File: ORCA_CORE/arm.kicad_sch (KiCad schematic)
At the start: 0 parts

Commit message: add power registers to power_board gate driver
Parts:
- added C10: 22u25V, Capacitor_SMD:C_0805_2012Metric_Pad1.18x1.45mm_HandSolder, symbol Device:C
- added C9: 10u/50V, Capacitor_SMD:C_1206_3216Metric_Pad1.33x1.80mm_HandSolder, symbol Device:C
- added D4: enable_arm, LED_SMD:LED_0603_1608Metric_Pad1.05x0.95mm_HandSolder, symbol Device:LED_Filled
- added D5: power_input_arm, LED_SMD:LED_0603_1608Metric_Pad1.05x0.95mm_HandSolder, symbol Device:LED_Filled
- added D6: CUHS20560, Diode:Diode_US2H, symbol Device:D_Schottky
- added J26: Vin_motor, Connector_JST:JST_XH_S2B-XH-A_1x02_P2.50mm_Horizontal, symbol Connector_Generic:Conn_01x02
- added J27: servo_0, symbol Connector:Conn_01x03_Pin
- added J28: servo_1, symbol Connector:Conn_01x03_Pin
- added J29: servo_2, symbol Connector:Conn_01x03_Pin
- added J30: servo_3, symbol Connector:Conn_01x03_Pin
- added Q3: TJ60S04M3L, toshiba:2-7M1A, symbol Simulation_SPICE:PMOS
- added R26: 10k, Resistor_SMD:R_0603_1608Metric_Pad0.98x0.95mm_HandSolder, symbol Device:R
- added R27, R28: 1k, Resistor_SMD:R_0603_1608Metric_Pad0.98x0.95mm_HandSolder, symbol Device:R
- added R29, R32, R39, R42, R45: 100, symbol Device:R
- added R30, R33, R36, R40, R41, R43, R44, R46, R50: 2.2k, symbol Device:R
- added R31: 47, symbol Device:R
- added U11, U12, U13, U15, U16: TLP293, Package_SO:SOIC-4_4.55x2.6mm_P1.27mm, symbol Isolator:TLP293
- added U17: AZ1117-3.3, Package_TO_SOT_SMD:SOT-223-3_TabPin2, symbol mylib:AZ1117-3.3V
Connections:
- new net: R29.2, R30.1, U11.1
- new net: J28.3 (Pin_3), U13.3
- new net: D5.2 (A), R28.1
- new net: R32.2, R33.1, U12.1
- new net: J27.3 (Pin_3), U12.3
- new net: R36.1, U12.4
- new net: R44.1, U15.4
- new net: D4.2 (A), R27.2
- new net: Q3.2 (G), R26.1, U11.3
- new net: R31.1, U11.4
- new net: R39.2, R40.1, U13.1
- new net: R41.1, U13.4
- new net: J30.3 (Pin_3), U16.3
- new net: R42.2, R43.1, U15.1
- new net: J29.3 (Pin_3), U15.3
- new net: R50.1, U16.4
- new net: R45.2, R46.1, U16.1
- new net +3V3: C10.1, D6.2 (A), R36.2, R41.2, R44.2, R50.2, U17.2 (Vout)
- new net +6V: J26.2 (Pin_2)
- new net +6V_in: C9.1, D6.1 (K), Q3.3 (S), R28.2, R31.2, U17.3 (Vin)
- new net +6V_out: J27.2 (Pin_2), J28.2 (Pin_2), J29.2 (Pin_2), J30.2 (Pin_2), Q3.1 (D), R27.1
- new net GND: C10.2, C9.2, D4.1 (K), D5.1 (K), J26.1 (Pin_1), J27.1 (Pin_1), J28.1 (Pin_1), J29.1 (Pin_1), J30.1 (Pin_1), R26.2, U17.1 (GND)
- new net GND1: U11.2, U12.2, U13.2, U15.2, U16.2
- new net Vin_cpu: R30.2, R33.2, R40.2, R43.2, R46.2
- new net enable_arm: R29.1
- new net servo_0: R32.1
- new net servo_1: R39.1
- new net servo_2: R42.1
- new net servo_3: R45.1
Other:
- note added: "4 motor inputs"
- note added: "enabler"
- note added: "power"
- note added: "regulator"

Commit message: almost completed CORE
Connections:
- net +6V is gone; now on net +6V_in: J26.2 (Pin_2)
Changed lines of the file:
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@@
 	)
 	(global_label "+6V_out"
-		(shape input)
+		(shape output)
 		(at 170.18 64.77 0)
 		(fields_autoplaced yes)
@@
 	)
 	(global_label "+3V3"
-		(shape input)
+		(shape output)
 		(at 259.08 41.91 0)
 		(fields_autoplaced yes)
@@
 		)
 	)
-	(global_label "+6V"
+	(global_label "+6V_in"
 		(shape input)
 		(at 53.34 71.12 0)
@@
 		)
 		(property "Intersheetrefs" "${INTERSHEET_REFS}"
-			(at 60.1957 71.12 0)
+			(at 62.9171 71.12 0)
 			(effects
 				(font

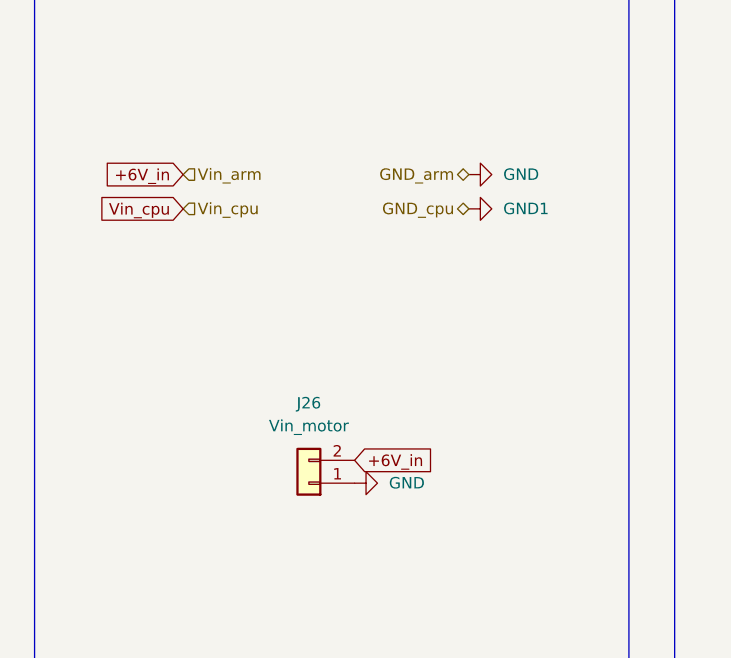
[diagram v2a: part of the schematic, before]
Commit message: complete attaching footprint of CORE
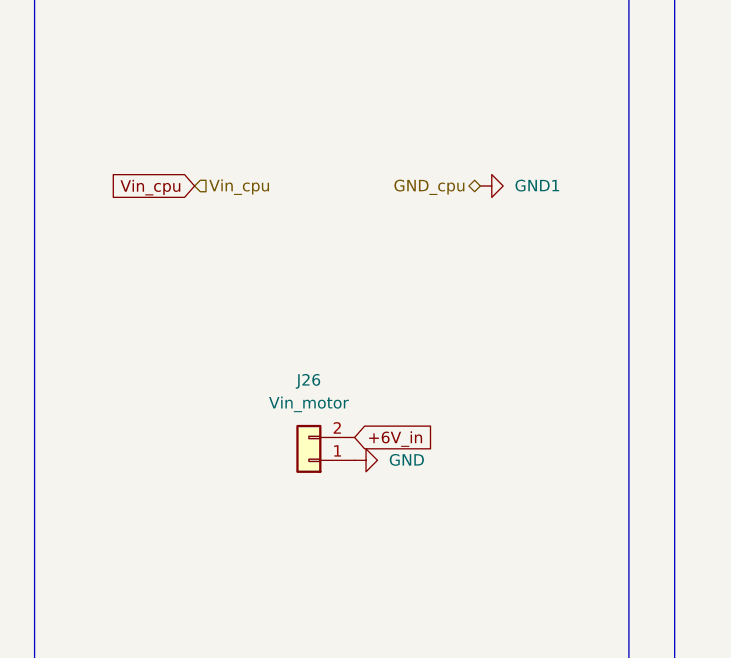
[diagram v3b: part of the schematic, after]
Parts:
- J27, J28, J29, J30: footprint (none) -> Connector_PinHeader_2.54mm:PinHeader_1x03_P2.54mm_Horizontal
- R29, R30, R31, R32, R33, R36, R39, R40, R41, R42, R43, R44, R45, R46, R50: footprint (none) -> Resistor_SMD:R_0603_1608Metric_Pad0.98x0.95mm_HandSolder
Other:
- moved on the sheet: J26
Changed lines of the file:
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@@
 	(global_label "Vin_cpu"
 		(shape input)
-		(at 34.29 43.18 180)
+		(at 35.56 40.64 180)
 		(fields_autoplaced yes)
 		(effects
@@
 		)
 		(property "Intersheetrefs" "${INTERSHEET_REFS}"
-			(at 24.1082 43.18 0)
+			(at 25.3782 40.64 0)
 			(effects
 				(font
@@
 		)
 	)
-	(global_label "+6V_in"
-		(shape input)
-		(at 34.29 39.37 180)
-		(fields_autoplaced yes)
-		(effects
-			(font
-				(size 1.27 1.27)
-			)
-			(justify right)
-		)
-		(property "Intersheetrefs" "${INTERSHEET_REFS}"
-			(at 24.7129 39.37 0)
-			(effects
-				(font
-					(size 1.27 1.27)
-				)
-				(justify right)
-				(hide yes)
-			)
-		)
-	)
 	(global_label "Vin_cpu"
 		(shape input)
@@
 	(global_label "+6V_in"
 		(shape input)
-		(at 53.34 71.12 0)
+		(at 53.34 68.58 0)
 		(fields_autoplaced yes)
 		(effects
@@
 		)
 		(property "Intersheetrefs" "${INTERSHEET_REFS}"
-			(at 62.9171 71.12 0)
+			(at 62.9171 68.58 0)
 			(effects
 				(font
@@
 		)
 	)
-	(hierarchical_label "GND_arm"
-		(shape bidirectional)
-		(at 66.04 39.37 180)
-		(fields_autoplaced yes)
-		(effects
-			(font
-				(size 1.27 1.27)
-			)
-			(justify right)
-		)
-	)
 	(hierarchical_label "GND_cpu"
 		(shape bidirectional)
-		(at 66.04 43.18 180)
+		(at 67.31 40.64 180)
 		(fields_autoplaced yes)
 		(effects
@@
 		)
 	)
-	(hierarchical_label "Vin_arm"
-		(shape input)
-		(at 34.29 39.37 0)
-		(fields_autoplaced yes)
-		(effects
-			(font
-				(size 1.27 1.27)
-			)
-			(justify left)
-		)
-	)
 	(hierarchical_label "Vin_cpu"
 		(shape input)
-		(at 34.29 43.18 0)
+		(at 35.56 40.64 0)
 		(fields_autoplaced yes)
 		(effects
@@
 			)
 		)
-		(property "Footprint" ""
+		(property "Footprint" "Resistor_SMD:R_0603_1608Metric_Pad0.98x0.95mm_HandSolder"
 			(at 131.318 35.56 90)
 			(effects
@@
 	(symbol
 		(lib_id "power:GND")
-		(at 66.04 39.37 90)
-		(unit 1)
-		(exclude_from_sim no)
-		(in_bom yes)
-		(on_board yes)
-		(dnp no)
-		(fields_autoplaced yes)
-		(property "Reference" "#PWR061"
-			(at 72.39 39.37 0)
-			(effects
-				(font
-					(size 1.27 1.27)
-				)
-				(hide yes)
-			)
-		)
-		(property "Value" "GND"
-			(at 69.85 39.3699 90)
-			(effects
-				(font
-					(size 1.27 1.27)
-				)
-				(justify right)
-			)
-		)
-		(property "Footprint" ""
-			(at 66.04 39.37 0)
-			(effects
-				(font
-					(size 1.27 1.27)
-				)
-				(hide yes)
-			)
-		)
-		(property "Datasheet" ""
-			(at 66.04 39.37 0)
-			(effects
-				(font
-					(size 1.27 1.27)
-				)
-				(hide yes)
-			)
-		)
-		(property "Description" "Power symbol creates a global label with name \"GND\" , ground"
-			(at 66.04 39.37 0)
-			(effects
-				(font
-					(size 1.27 1.27)
-				)
-				(hide yes)
-			)
-		)
-		(pin "1"
-		)
-		(instances
-			(project "ORCA_CORE"
-				(path "/895d6bb7-4008-488b-a34b-0077e9f7e4a1/f4046d1b-97e2-423b-a39b-40122b0e9f7a"
-					(reference "#PWR061")
-					(unit 1)
-				)
-			)
-		)
-	)
-	(symbol
-		(lib_id "power:GND")
 		(at 215.9 154.94 270)
 		(unit 1)
@@
 			)
 		)
-		(property "Footprint" ""
+		(property "Footprint" "Connector_PinHeader_2.54mm:PinHeader_1x03_P2.54mm_Horizontal"
 			(at 116.84 152.4 0)
 			(effects
@@
 			)
 		)
-		(property "Footprint" ""
+		(property "Footprint" "Resistor_SMD:R_0603_1608Metric_Pad0.98x0.95mm_HandSolder"
 			(at 208.28 118.618 90)
 			(effects
@@
 			)
 		)
-		(property "Footprint" ""
+		(property "Footprint" "Resistor_SMD:R_0603_1608Metric_Pad0.98x0.95mm_HandSolder"
 			(at 123.19 43.688 90)
 			(effects
@@
 			)
 		)
-		(property "Footprint" ""
+		(property "Footprint" "Resistor_SMD:R_0603_1608Metric_Pad0.98x0.95mm_HandSolder"
 			(at 83.058 110.49 90)
 			(effects
@@
 			)
 		)
-		(property "Footprint" ""
+		(property "Footprint" "Resistor_SMD:R_0603_1608Metric_Pad0.98x0.95mm_HandSolder"
 			(at 152.4 43.688 90)
 			(effects
@@
 			)
 		)
-		(property "Footprint" ""
+		(property "Footprint" "Resistor_SMD:R_0603_1608Metric_Pad0.98x0.95mm_HandSolder"
 			(at 74.93 118.618 90)
 			(effects
@@
 			)
 		)
-		(property "Footprint" ""
+		(property "Footprint" "Connector_PinHeader_2.54mm:PinHeader_1x03_P2.54mm_Horizontal"
 			(at 220.98 152.4 0)
 			(effects
@@
 	(symbol
 		(lib_id "power:GND1")
-		(at 66.04 43.18 90)
+		(at 67.31 40.64 90)
 		(unit 1)
 		(exclude_from_sim no)
@@
 		(fields_autoplaced yes)
 		(property "Reference" "#PWR062"
-			(at 72.39 43.18 0)
+			(at 73.66 40.64 0)
 			(effects
 				(font
@@
 		)
 		(property "Value" "GND1"
-			(at 69.85 43.1799 90)
+			(at 71.12 40.6399 90)
 			(effects
 				(font
@@
 		)
 		(property "Footprint" ""
-			(at 66.04 43.18 0)
+			(at 67.31 40.64 0)
 			(effects
 				(font
@@
 		)
 		(property "Datasheet" ""
-			(at 66.04 43.18 0)
+			(at 67.31 40.64 0)
 			(effects
 				(font
@@
 		)
 		(property "Description" "Power symbol creates a global label with name \"GND1\" , ground"
-			(at 66.04 43.18 0)
+			(at 67.31 40.64 0)
 			(effects
 				(font
@@
 			)
 		)
-		(property "Footprint" ""
+		(property "Footprint" "Resistor_SMD:R_0603_1608Metric_Pad0.98x0.95mm_HandSolder"
 			(at 74.93 146.558 90)
 			(effects
@@
 			)
 		)
-		(property "Footprint" ""
+		(property "Footprint" "Connector_PinHeader_2.54mm:PinHeader_1x03_P2.54mm_Horizontal"
 			(at 220.98 124.46 0)
 			(effects
@@
 			)
 		)
-		(property "Footprint" ""
+		(property "Footprint" "Resistor_SMD:R_0603_1608Metric_Pad0.98x0.95mm_HandSolder"
 			(at 208.28 146.558 90)
 			(effects
@@
 	(symbol
 		(lib_id "power:GND")
-		(at 53.34 73.66 90)
+		(at 53.34 71.12 90)
 		(unit 1)
 		(exclude_from_sim no)
@@
 		(fields_autoplaced yes)
 		(property "Reference" "#PWR060"
-			(at 59.69 73.66 0)
+			(at 59.69 71.12 0)
 			(effects
 				(font
@@
 		)
 		(property "Value" "GND"
-			(at 57.15 73.6599 90)
+			(at 57.15 71.1199 90)
 			(effects
 				(font
@@
 		)
 		(property "Footprint" ""
-			(at 53.34 73.66 0)
+			(at 53.34 71.12 0)
 			(effects
 				(font
@@
 		)
 		(property "Datasheet" ""
-			(at 53.34 73.66 0)
+			(at 53.34 71.12 0)
 			(effects
 				(font
@@
 		)
 		(property "Description" "Power symbol creates a global label with name \"GND\" , ground"
-			(at 53.34 73.66 0)
+			(at 53.34 71.12 0)
 			(effects
 				(font
@@
 			)
 		)
-		(property "Footprint" ""
+		(property "Footprint" "Resistor_SMD:R_0603_1608Metric_Pad0.98x0.95mm_HandSolder"
 			(at 179.07 146.558 90)
 			(effects
@@
 			)
 		)
-		(property "Footprint" ""
+		(property "Footprint" "Resistor_SMD:R_0603_1608Metric_Pad0.98x0.95mm_HandSolder"
 			(at 187.198 138.43 90)
 			(effects
@@
 			)
 		)
-		(property "Footprint" ""
+		(property "Footprint" "Resistor_SMD:R_0603_1608Metric_Pad0.98x0.95mm_HandSolder"
 			(at 104.14 146.558 90)
 			(effects
@@
 	(symbol
 		(lib_id "Connector_Generic:Conn_01x02")
-		(at 48.26 73.66 180)
+		(at 48.26 71.12 180)
 		(unit 1)
 		(exclude_from_sim no)
@@
 		(fields_autoplaced yes)
 		(property "Reference" "J26"
-			(at 48.26 64.77 0)
+			(at 48.26 62.23 0)
 			(effects
 				(font
@@
 		)
 		(property "Value" "Vin_motor"
-			(at 48.26 67.31 0)
+			(at 48.26 64.77 0)
 			(effects
 				(font
@@
 		)
 		(property "Footprint" "Connector_JST:JST_XH_S2B-XH-A_1x02_P2.50mm_Horizontal"
-			(at 48.26 73.66 0)
+			(at 48.26 71.12 0)
 			(effects
 				(font
@@
 		)
 		(property "Datasheet" "~"
-			(at 48.26 73.66 0)
+			(at 48.26 71.12 0)
 			(effects
 				(font
@@
 		)
 		(property "Description" "Generic connector, single row, 01x02, script generated (kicad-library-utils/schlib/autogen/connector/)"
-			(at 48.26 73.66 0)
+			(at 48.26 71.12 0)
 			(effects
 				(font
@@
 			)
 		)
-		(property "Footprint" ""
+		(property "Footprint" "Resistor_SMD:R_0603_1608Metric_Pad0.98x0.95mm_HandSolder"
 			(at 179.07 118.618 90)
 			(effects
@@
 			)
 		)
-		(property "Footprint" ""
+		(property "Footprint" "Connector_PinHeader_2.54mm:PinHeader_1x03_P2.54mm_Horizontal"
 			(at 116.84 124.46 0)
 			(effects
@@
 			)
 		)
-		(property "Footprint" ""
+		(property "Footprint" "Resistor_SMD:R_0603_1608Metric_Pad0.98x0.95mm_HandSolder"
 			(at 104.14 118.618 90)
 			(effects
@@
 			)
 		)
-		(property "Footprint" ""
+		(property "Footprint" "Resistor_SMD:R_0603_1608Metric_Pad0.98x0.95mm_HandSolder"
 			(at 187.198 110.49 90)
 			(effects
@@
 			)
 		)
-		(property "Footprint" ""
+		(property "Footprint" "Resistor_SMD:R_0603_1608Metric_Pad0.98x0.95mm_HandSolder"
 			(at 83.058 138.43 90)
 			(effects

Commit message: place most of footprints. test replicate
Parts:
- J27, J28, J29, J30: footprint Connector_PinHeader_2.54mm:PinHeader_1x03_P2.54mm_Horizontal -> Connector_PinHeader_2.54mm:PinHeader_1x03_P2.54mm_Vertical
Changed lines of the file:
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@@
 			)
 		)
-		(property "Footprint" "Connector_PinHeader_2.54mm:PinHeader_1x03_P2.54mm_Horizontal"
+		(property "Footprint" "Connector_PinHeader_2.54mm:PinHeader_1x03_P2.54mm_Vertical"
 			(at 116.84 152.4 0)
 			(effects
@@
 			)
 		)
-		(property "Footprint" "Connector_PinHeader_2.54mm:PinHeader_1x03_P2.54mm_Horizontal"
+		(property "Footprint" "Connector_PinHeader_2.54mm:PinHeader_1x03_P2.54mm_Vertical"
 			(at 220.98 152.4 0)
 			(effects
@@
 			)
 		)
-		(property "Footprint" "Connector_PinHeader_2.54mm:PinHeader_1x03_P2.54mm_Horizontal"
+		(property "Footprint" "Connector_PinHeader_2.54mm:PinHeader_1x03_P2.54mm_Vertical"
 			(at 220.98 124.46 0)
 			(effects
@@
 			)
 		)
-		(property "Footprint" "Connector_PinHeader_2.54mm:PinHeader_1x03_P2.54mm_Horizontal"
+		(property "Footprint" "Connector_PinHeader_2.54mm:PinHeader_1x03_P2.54mm_Vertical"
 			(at 116.84 124.46 0)
 			(effects

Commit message: most of wire placed. try update kicad to use replicate library
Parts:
- removed J27: servo_0, Connector_PinHeader_2.54mm:PinHeader_1x03_P2.54mm_Vertical, symbol Connector:Conn_01x03_Pin
- removed J28: servo_1, Connector_PinHeader_2.54mm:PinHeader_1x03_P2.54mm_Vertical, symbol Connector:Conn_01x03_Pin
- removed J29: servo_2, Connector_PinHeader_2.54mm:PinHeader_1x03_P2.54mm_Vertical, symbol Connector:Conn_01x03_Pin
- removed J30: servo_3, Connector_PinHeader_2.54mm:PinHeader_1x03_P2.54mm_Vertical, symbol Connector:Conn_01x03_Pin
- added H25, H26: Hole_arm, MountingHole:MountingHole_3.2mm_M3, symbol Mechanical:MountingHole
- added J55: servo connectors, Conn:PinHeader_03x04_P2.54mm_Vertical, symbol Connector:Conn_01x12_Pin
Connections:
- net +6V_out: now also J55.11 (Pin_11), J55.2 (Pin_2), J55.5 (Pin_5), J55.8 (Pin_8)
- net GND: now also J55.1 (Pin_1), J55.10 (Pin_10), J55.4 (Pin_4), J55.7 (Pin_7)
- net servo_0: now also R39.1; no longer R32.1
- net servo_1: now also R32.1; no longer R39.1
- net at U13.3: now also J55.12 (Pin_12)
- net at U12.3: now also J55.9 (Pin_9)
- net at U16.3: now also J55.3 (Pin_3)
- net at U15.3: now also J55.6 (Pin_6)
- net Vin_cpu renamed Vin_arm
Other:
- moved on the sheet: R32, R33, R36, R39, R40, R41, R42, R43, R44, R45, R46, R50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
